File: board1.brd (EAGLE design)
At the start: 45 x 35 mm, 11 parts

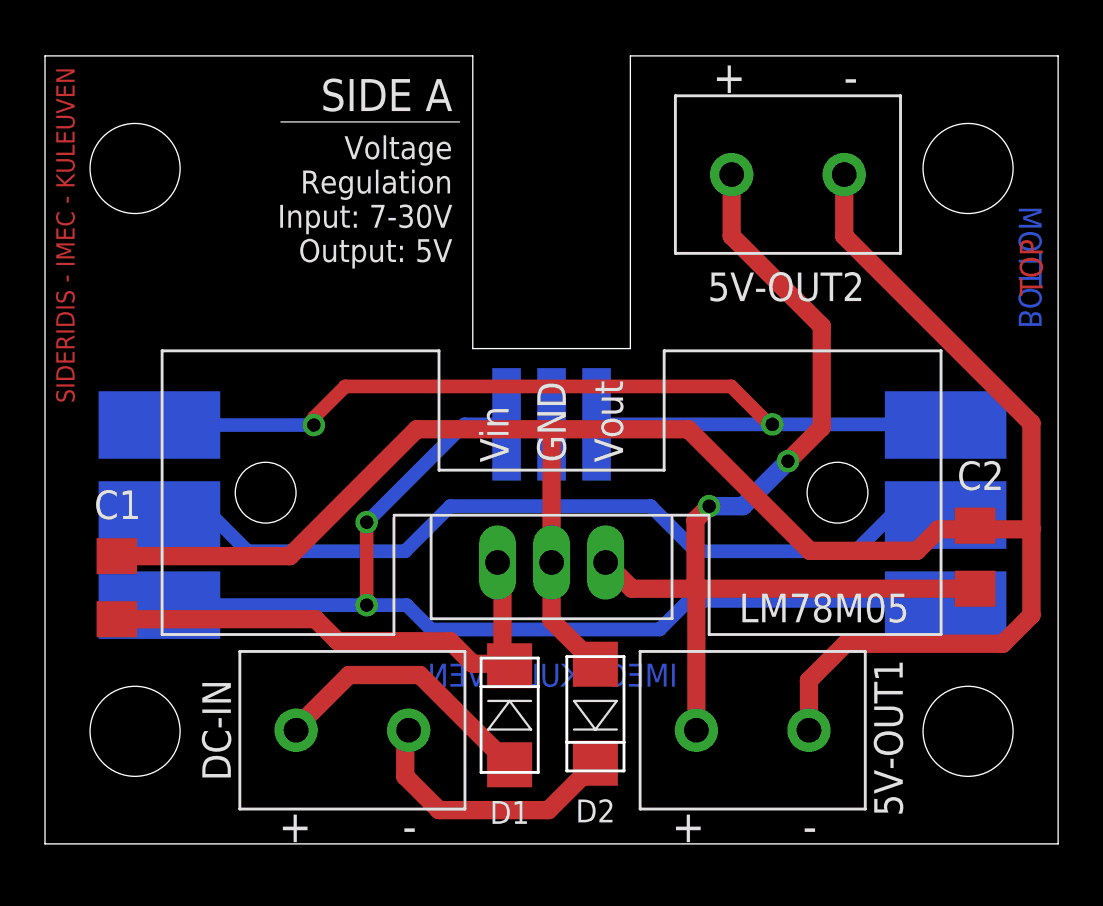
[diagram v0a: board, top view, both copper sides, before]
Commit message: Fixed the wrong path for bypass caps. Version v1.1
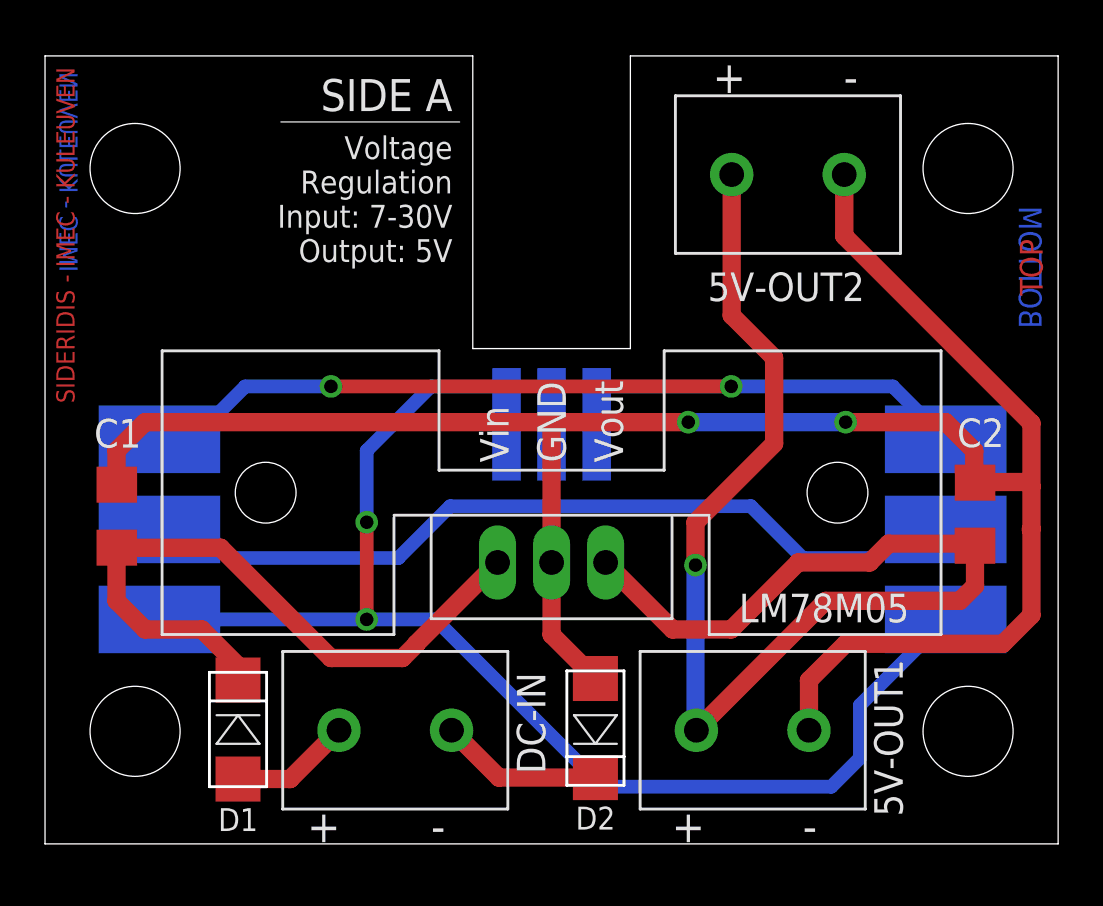
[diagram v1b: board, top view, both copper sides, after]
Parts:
- moved D1 12.1 mm to (8.57, 5.08)
- moved C1 3.17 mm to (3.19, 14.6)
- moved C2 1.91 mm to (41.3, 14.6)
- moved DC-IN 1.90 mm to (15.6, 5.05)
- moved D2 0.64 mm to (24.4, 5.14)
- moved BUS1 0.63 mm to (40.0, 14.0)
- moved BUS2 0.63 mm to (5.08, 14.0)
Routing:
- net 5V: track 46.5 -> 63.0 mm, vias 2 -> 1
- net S_VDD: track 47.7 -> 59.9 mm
- net N$2: track 23.1 -> 30.3 mm
- net VIN: track 12.2 -> 5.38 mm
- net N$4: track 12.0 -> 7.26 mm
- net S_GND: track 44.4 -> 45.8 mm
- net S_DQ: track 41.6 -> 42.9 mm
- net GND: track 93.4 -> 93.0 mm, vias 0 -> 2
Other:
- board text added: "Paschalis Sideridis April 2016 v1.1"
- board text removed: "Paschalis Sideridis April 2016 v1.0"
